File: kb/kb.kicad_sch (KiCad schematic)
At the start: 109 parts, among them J1 Conn_01x04_MountingPin, SW1 SW_Push, SW10 SW_Push, SW11 SW_Push, SW12 SW_Push, SW13 SW_Push, SW14 SW_Push, SW15 SW_Push, SW16 SW_Push, SW17 SW_Push, SW18 SW_Push, SW19 SW_Push, SW2 SW_Push, SW20 SW_Push, SW21 SW_Push, SW22 SW_Push, SW23 SW_Push, SW24 SW_Push, SW25 SW_Push, SW26 SW_Push, SW27 SW_Push, SW28 SW_Push, SW29 SW_Push, SW3 SW_Push, SW30 SW_Push, SW31 SW_Push, SW32 SW_Push, SW33 SW_Push, SW34 SW_Push, SW35 SW_Push, SW36 SW_Push, SW37 SW_Push, SW38 SW_Push, SW39 SW_Push, SW4 SW_Push, SW40 SW_Push, SW41 SW_Push, SW42 SW_Push, SW43 SW_Push, SW44 SW_Push, SW45 SW_Push, SW46 SW_Push, SW48 SW_Push, SW5 SW_Push, SW6 SW_Push, SW7 SW_Push, SW8 SW_Push, SW9 SW_Push, U1 USBLC6-2SC6, U2 STM32G474CETx, U4 XC6206PxxxMR

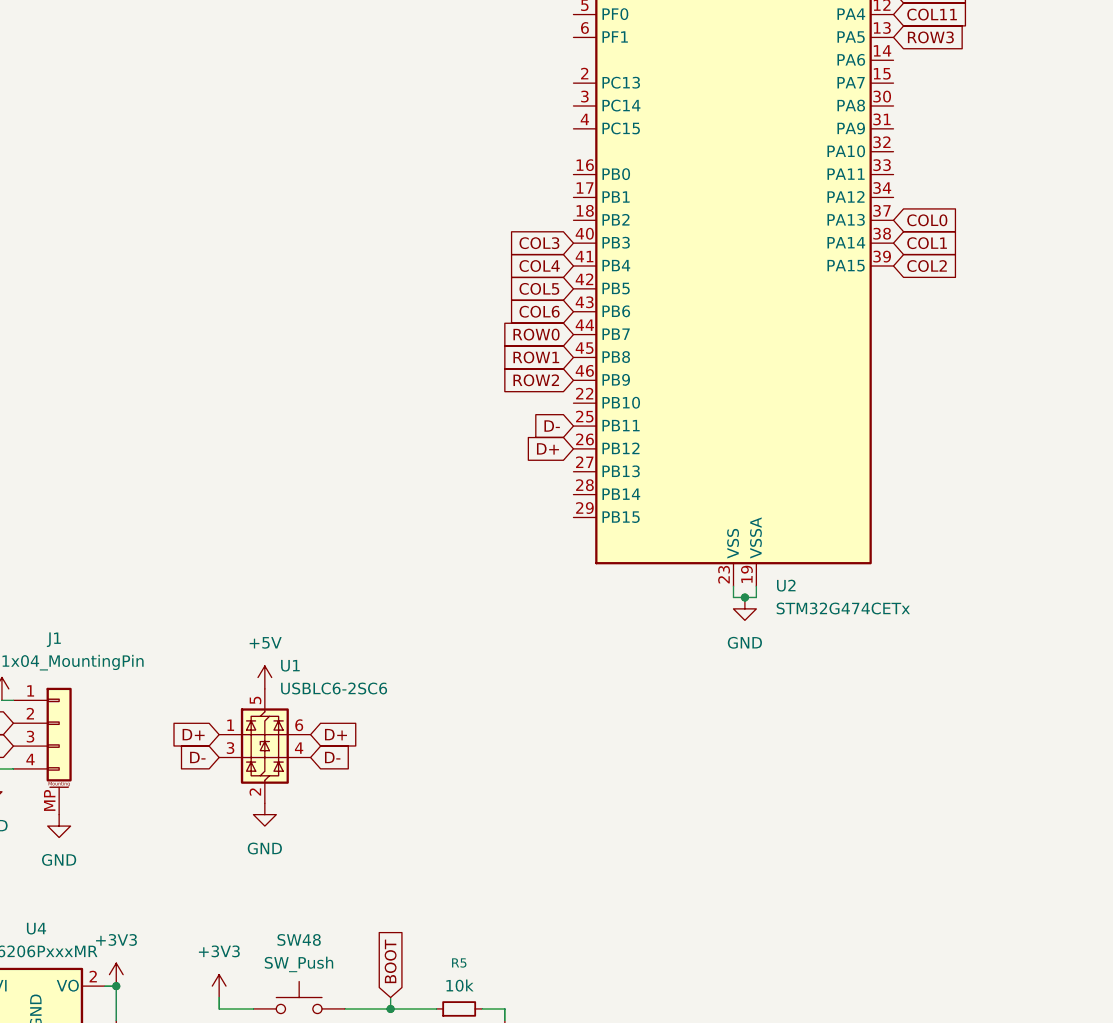
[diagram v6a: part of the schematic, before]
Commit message: Removed ESD component
Due to built-in ESD functionality on daughterboard, onboard ESD protection is unnecessary
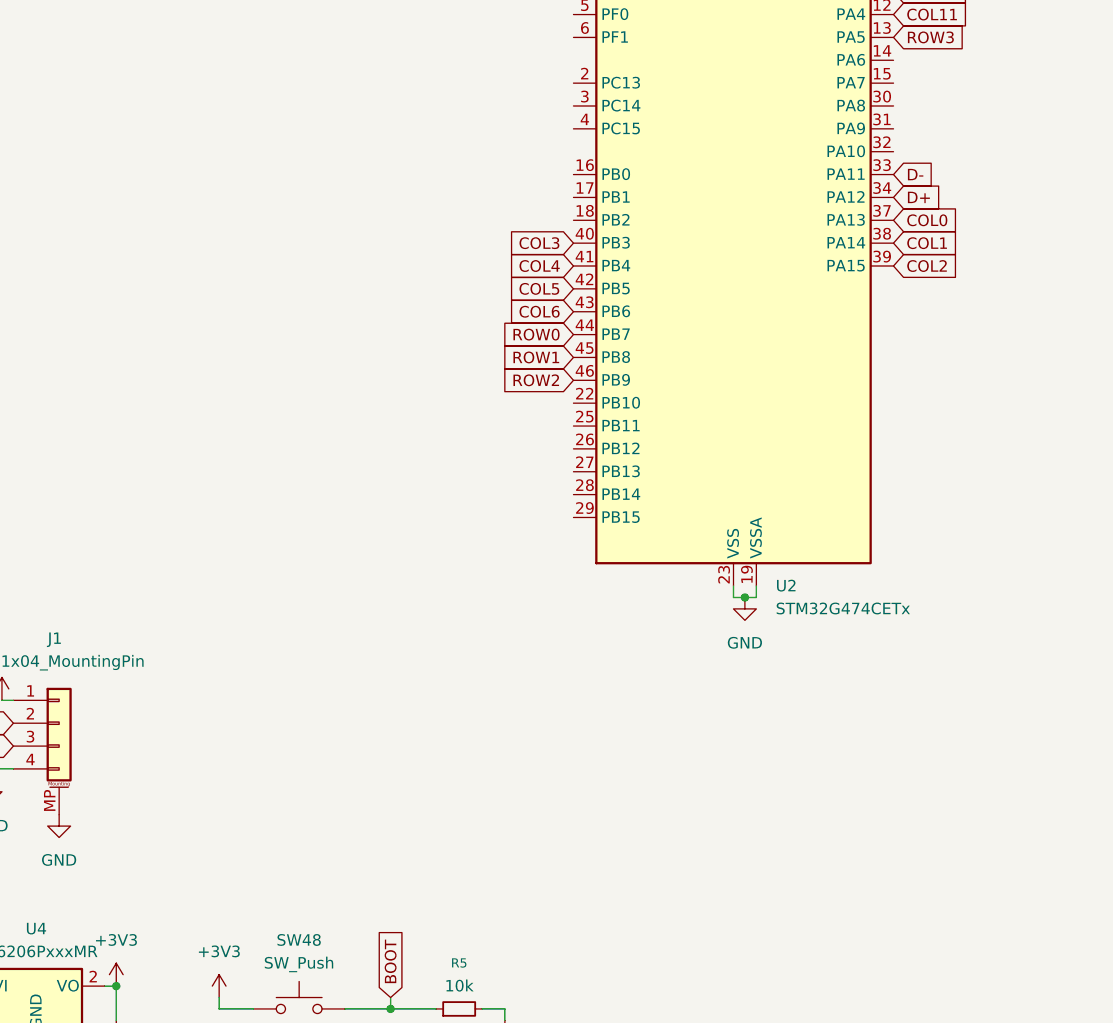
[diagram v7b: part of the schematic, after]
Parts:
- removed U1: USBLC6-2SC6, Package_TO_SOT_SMD:SOT-23-6, symbol Power_Protection:USBLC6-2SC6
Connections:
- net D+: now also U2.34 (PA12); no longer U2.26 (PB12)
- net D-: now also U2.33 (PA11); no longer U2.25 (PB11)
